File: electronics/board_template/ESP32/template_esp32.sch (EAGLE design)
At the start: 51 parts, among them IC1 ESP-WROOM-32D, IC2 CP2104-F03-GMR, IC3 NCP1117ST50T3G, IC4 LMV358IDGKRG4, IC5 NCP1117ST33T3G, J1 GROVE_CONNECTOR2.0_1X4, J2 GROVE_CONNECTOR2.0_1X4, J4 10129383-912001ALF, J5 10129383-912001ALF, Q1 FDN340P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

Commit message: Logo hinzugefügt
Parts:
- added U$1: LOGO_MORPHBOT3MM, topo-eng:LOGO_MORPHBOT3MM
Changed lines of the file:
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@@
 <layer number="104" name="Name" color="7" fill="1" visible="no" active="yes"/>
 <layer number="116" name="Patch_BOT" color="9" fill="4" visible="no" active="yes"/>
+<layer number="120" name="brd_placement_notes" color="7" fill="1" visible="yes" active="yes"/>
 <layer number="121" name="_tsilk" color="7" fill="1" visible="no" active="yes"/>
 <layer number="122" name="_bsilk" color="7" fill="1" visible="no" active="yes"/>
+<layer number="144" name="DrillLegend" color="7" fill="1" visible="yes" active="yes"/>
+<layer number="145" name="DrillLegend_01-16" color="7" fill="1" visible="yes" active="yes"/>
+<layer number="146" name="DrillLegend_01-20" color="7" fill="1" visible="yes" active="yes"/>
 <layer number="151" name="HeatSink" color="14" fill="1" visible="no" active="no"/>
+<layer number="198" name="BMP198" color="7" fill="1" visible="yes" active="yes"/>
+<layer number="199" name="Contour" color="7" fill="1" visible="yes" active="yes"/>
 <layer number="200" name="200bmp" color="1" fill="10" visible="no" active="no"/>
 <layer number="201" name="201bmp" color="2" fill="1" visible="no" active="no"/>
@@
 <layer number="207" name="207bmp" color="15" fill="10" visible="no" active="no"/>
 <layer number="208" name="208bmp" color="9" fill="10" visible="no" active="yes"/>
+<layer number="209" name="Route9Document" color="7" fill="1" visible="yes" active="yes"/>
+<layer number="210" name="Route10Document" color="7" fill="1" visible="yes" active="yes"/>
+<layer number="211" name="Route11Document" color="7" fill="1" visible="yes" active="yes"/>
+<layer number="212" name="Route12Document" color="7" fill="1" visible="yes" active="yes"/>
+<layer number="213" name="Route13Document" color="7" fill="1" visible="yes" active="yes"/>
+<layer number="214" name="Route14Document" color="7" fill="1" visible="yes" active="yes"/>
+<layer number="215" name="Route15Document" color="7" fill="1" visible="yes" active="yes"/>
+<layer number="216" name="BottomDocument" color="7" fill="1" visible="yes" active="yes"/>
+<layer number="220" name="DimensionDocument" color="7" fill="1" visible="yes" active="yes"/>
+<layer number="221" name="tPlaceDocument" color="7" fill="1" visible="yes" active="yes"/>
+<layer number="222" name="bPlaceDocument" color="7" fill="1" visible="yes" active="yes"/>
+<layer number="225" name="tNamesDocument" color="7" fill="1" visible="yes" active="yes"/>
+<layer number="226" name="bNamesDocument" color="7" fill="1" visible="yes" active="yes"/>
+<layer number="227" name="tValuesDocument" color="7" fill="1" visible="yes" active="yes"/>
+<layer number="228" name="bValuesDocument" color="7" fill="1" visible="yes" active="yes"/>
+<layer number="229" name="tStopDocument" color="7" fill="1" visible="yes" active="yes"/>
+<layer number="230" name="bStopDocument" color="7" fill="1" visible="yes" active="yes"/>
+<layer number="231" name="tCreamDocument" color="7" fill="1" visible="yes" active="yes"/>
+<layer number="232" name="bCreamDocument" color="7" fill="1" visible="yes" active="yes"/>
+<layer number="233" name="tFinishDocument" color="7" fill="1" visible="yes" active="yes"/>
+<layer number="234" name="bFinishDocument" color="7" fill="1" visible="yes" active="yes"/>
+<layer number="235" name="tGlueDocument" color="7" fill="1" visible="yes" active="yes"/>
+<layer number="236" name="bGlueDocument" color="7" fill="1" visible="yes" active="yes"/>
+<layer number="244" name="DrillsDocument" color="7" fill="1" visible="yes" active="yes"/>
+<layer number="245" name="HolesDocument" color="7" fill="1" visible="yes" active="yes"/>
+<layer number="246" name="MillingDocument" color="7" fill="1" visible="yes" active="yes"/>
+<layer number="247" name="MeasuresDocument" color="7" fill="1" visible="yes" active="yes"/>
 <layer number="250" name="Descript" color="3" fill="1" visible="no" active="no"/>
 <layer number="251" name="SMDround" color="12" fill="11" visible="no" active="no"/>
@@
 <part name="LED2" library="led" library_urn="urn:adsk.eagle:library:259" deviceset="LED" device="CHIPLED_0603" package3d_urn="urn:adsk.eagle:package:15822/2" value="Everlight Elec 19-217/GHC-YR1S2/3T"/>
 <part name="R18" library="rcl" library_urn="urn:adsk.eagle:library:334" deviceset="R-EU_" device="R0402" package3d_urn="urn:adsk.eagle:package:23547/3" value="Uniroyal Elec 0402WGF4700TCE - 470"/>
+<part name="U$1" library="topo-eng" library_urn="urn:adsk.eagle:library:6646478" deviceset="LOGO_MORPHBOT" device="3MM"/>
 </parts>
 <sheets>
@@
 <attribute name="VALUE" x="205.74" y="85.598" size="1.778" layer="96"/>
 </instance>
+<instance part="U$1" gate="G$1" x="66.04" y="66.04" smashed="yes"/>
 </instances>
 <busses>

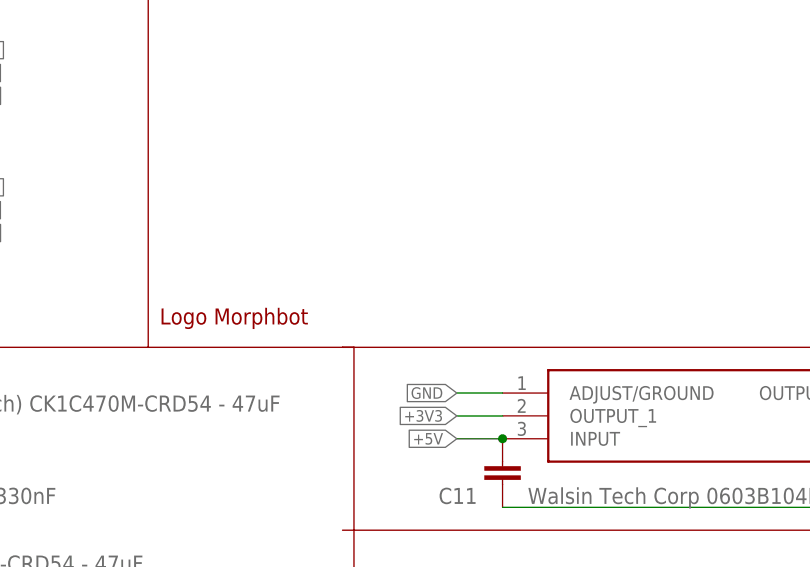
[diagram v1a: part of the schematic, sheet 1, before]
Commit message: Fiducials eingefügt
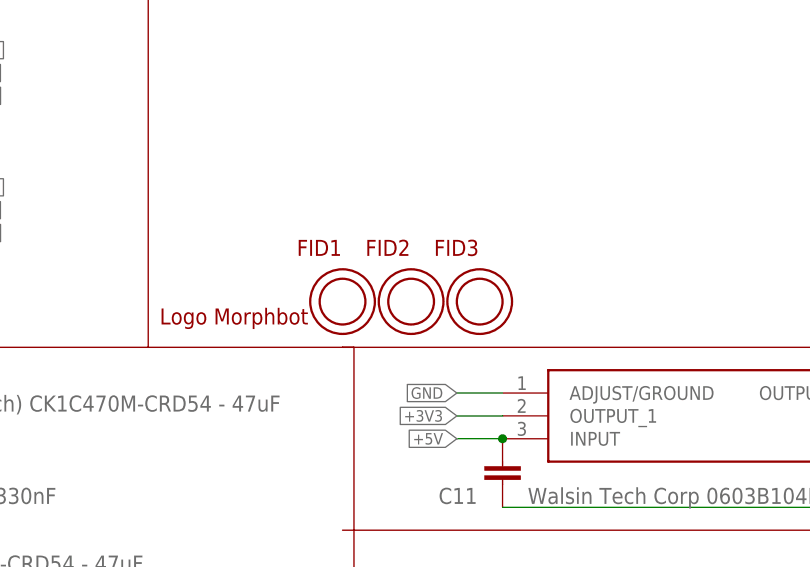
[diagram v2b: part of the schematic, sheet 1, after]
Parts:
- added FID1, FID2, FID3: OPEN-PNP-FIDUCIAL, topo-eng:OPEN-PNP-FIDUCIAL
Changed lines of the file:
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@@
 <part name="R18" library="rcl" library_urn="urn:adsk.eagle:library:334" deviceset="R-EU_" device="R0402" package3d_urn="urn:adsk.eagle:package:23547/3" value="Uniroyal Elec 0402WGF4700TCE - 470"/>
 <part name="U$1" library="topo-eng" library_urn="urn:adsk.eagle:library:6646478" deviceset="LOGO_MORPHBOT" device="3MM"/>
+<part name="FID1" library="topo-eng" library_urn="urn:adsk.eagle:library:6646478" deviceset="OPEN-PNP-FIDUCIAL" device=""/>
+<part name="FID2" library="topo-eng" library_urn="urn:adsk.eagle:library:6646478" deviceset="OPEN-PNP-FIDUCIAL" device=""/>
+<part name="FID3" library="topo-eng" library_urn="urn:adsk.eagle:library:6646478" deviceset="OPEN-PNP-FIDUCIAL" device=""/>
 </parts>
 <sheets>
@@
 </instance>
 <instance part="U$1" gate="G$1" x="66.04" y="66.04" smashed="yes"/>
+<instance part="FID1" gate="FID$1" x="86.36" y="68.58" smashed="yes">
+<attribute name="NAME" x="81.28" y="73.66" size="1.778" layer="94"/>
+</instance>
+<instance part="FID2" gate="FID$1" x="93.98" y="68.58" smashed="yes">
+<attribute name="NAME" x="88.9" y="73.66" size="1.778" layer="94"/>
+</instance>
+<instance part="FID3" gate="FID$1" x="101.6" y="68.58" smashed="yes">
+<attribute name="NAME" x="96.52" y="73.66" size="1.778" layer="94"/>
+</instance>
 </instances>
 <busses>

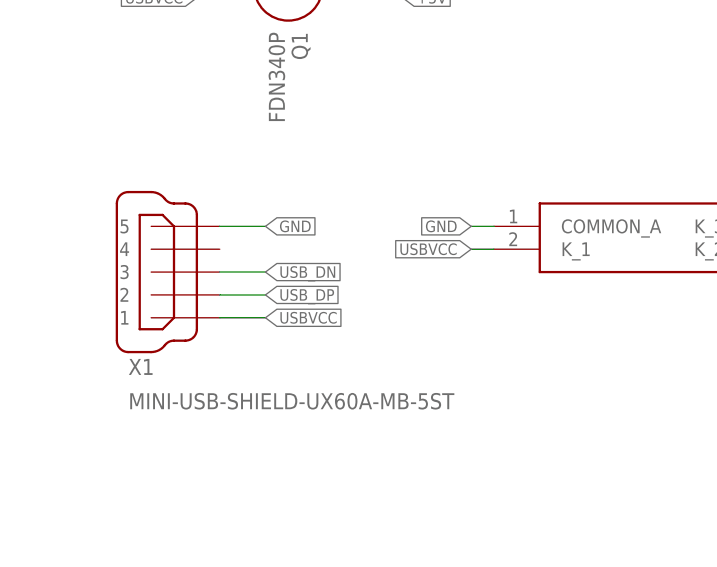
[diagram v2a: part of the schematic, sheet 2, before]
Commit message: ESP32-Template: - USB-Datenleitungen getauscht (BugFix) 328P-Template: - USB-Datenleitungen getauscht (BugFix) - Reset-Leitung mit DTR verbunden (Zum Programieren über ARDUINO-IDE notwendig)
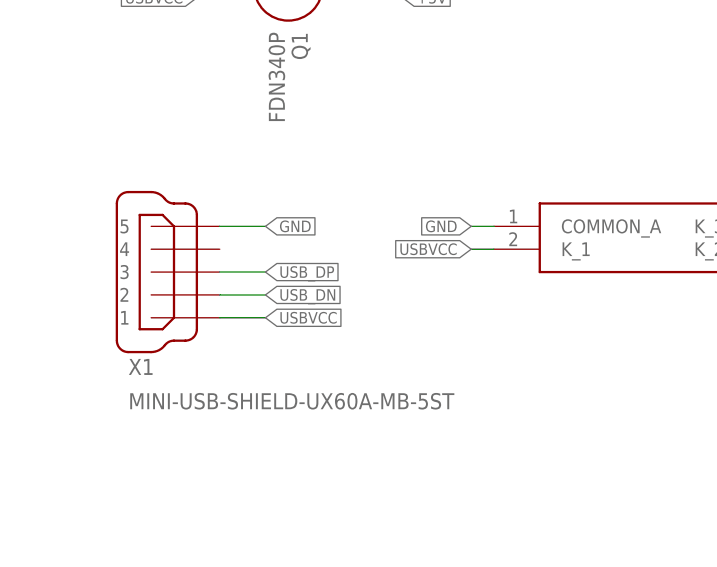
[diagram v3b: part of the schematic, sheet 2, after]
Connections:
- net USB_DN: now also X1G$1.2; no longer X1G$1.3
- net USB_DP: now also X1G$1.3; no longer X1G$1.2
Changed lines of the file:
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@@
 <net name="USB_DP" class="0">
-<segment>
-<pinref part="X1" gate="G$1" pin="2"/>
-<wire x1="22.86" y1="22.86" x2="27.94" y2="22.86" width="0.1524" layer="91"/>
-<label x="27.94" y="22.86" size="1.27" layer="95" ratio="5" xref="yes"/>
-</segment>
 <segment>
 <pinref part="D1" gate="G$1" pin="K_2"/>
@@
 <label x="121.92" y="91.44" size="1.27" layer="95" ratio="5" rot="R180" xref="yes"/>
 </segment>
-</net>
-<net name="USB_DN" class="0">
 <segment>
 <pinref part="X1" gate="G$1" pin="3"/>
@@
 <label x="27.94" y="25.4" size="1.27" layer="95" ratio="5" xref="yes"/>
 </segment>
+</net>
+<net name="USB_DN" class="0">
 <segment>
 <pinref part="D1" gate="G$1" pin="K_3"/>
@@
 <label x="121.92" y="88.9" size="1.27" layer="95" ratio="5" rot="R180" xref="yes"/>
 </segment>
+<segment>
+<pinref part="X1" gate="G$1" pin="2"/>
+<wire x1="22.86" y1="22.86" x2="27.94" y2="22.86" width="0.1524" layer="91"/>
+<label x="27.94" y="22.86" size="1.27" layer="95" ratio="5" xref="yes"/>
+</segment>
 </net>
